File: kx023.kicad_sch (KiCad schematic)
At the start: 5 parts, among them U2001 KX023-1025-FR

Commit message: Schematic Changes
Added Manufacturer/MPN/Description Fields to parts
Added libraries to project
Modified FMC schematic to use new symbol
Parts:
- R2001, R2002: Manufacturer (none) -> YAGEO; Manufacturer Part Number (none) -> RC0603FR-074K75L
- U2001: Manufacturer (none) -> Kionix; Manufacturer Part Number (none) -> KX023-1025-FR
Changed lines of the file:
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@@
 			)
 		)
-		(property "Description" "Resistor"
+		(property "Description" "RES 4.75K OHM 1% 1/10W 0603"
 			(at 124.46 73.66 0)
 			(effects
@@
 		(property "Vendor" "digikey:311-4.75KHRCT-ND"
 			(at 248.92 0 0)
+			(effects
+				(font
+					(size 1.27 1.27)
+				)
+				(hide yes)
+			)
+		)
+		(property "Manufacturer" "YAGEO "
+			(at 124.46 73.66 0)
+			(effects
+				(font
+					(size 1.27 1.27)
+				)
+				(hide yes)
+			)
+		)
+		(property "Manufacturer Part Number" "RC0603FR-074K75L "
+			(at 124.46 73.66 0)
 			(effects
 				(font
@@
 			)
 		)
-		(property "Description" "Resistor"
+		(property "Description" "RES 4.75K OHM 1% 1/10W 0603"
 			(at 119.38 73.66 0)
 			(effects
@@
 		(property "Vendor" "digikey:311-4.75KHRCT-ND"
 			(at 238.76 0 0)
+			(effects
+				(font
+					(size 1.27 1.27)
+				)
+				(hide yes)
+			)
+		)
+		(property "Manufacturer" "YAGEO "
+			(at 119.38 73.66 0)
+			(effects
+				(font
+					(size 1.27 1.27)
+				)
+				(hide yes)
+			)
+		)
+		(property "Manufacturer Part Number" "RC0603FR-074K75L "
+			(at 119.38 73.66 0)
 			(effects
 				(font
@@
 			)
 		)
-		(property "Description" ""
+		(property "Description" "ACCELEROMETER 2-8G I2C/SPI 16LGA"
 			(at 139.7 82.55 0)
 			(effects
@@
 		(property "Vendor" "digikey:1191-1039-1-ND"
 			(at 0 165.1 0)
+			(effects
+				(font
+					(size 1.27 1.27)
+				)
+				(hide yes)
+			)
+		)
+		(property "Manufacturer" "Kionix"
+			(at 139.7 82.55 0)
+			(effects
+				(font
+					(size 1.27 1.27)
+				)
+				(hide yes)
+			)
+		)
+		(property "Manufacturer Part Number" "KX023-1025-FR "
+			(at 139.7 82.55 0)
 			(effects
 				(font
@@
 			)
 		)
+		(property "Manufacturer" ""
+			(at 109.22 83.82 0)
+			(effects
+				(font
+					(size 1.27 1.27)
+				)
+				(hide yes)
+			)
+		)
+		(property "Manufacturer Part Number" ""
+			(at 109.22 83.82 0)
+			(effects
+				(font
+					(size 1.27 1.27)
+				)
+				(hide yes)
+			)
+		)
 		(pin "1"
 		)
@@
 			(at 109.22 81.28 0)
 			(effects
+				(font
+					(size 1.27 1.27)
+				)
+				(hide yes)
+			)
+		)
+		(property "Manufacturer" ""
+			(at 109.22 81.28 0)
+			(effects
+				(font
+					(size 1.27 1.27)
+				)
+				(hide yes)
+			)
+		)
+		(property "Manufacturer Part Number" ""
+			(at 109.22 81.28 0)
+			(effects

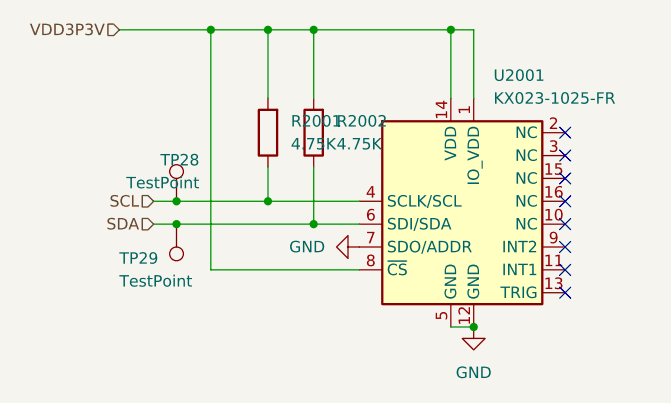
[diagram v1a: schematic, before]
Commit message: Properly attributed DNP parts; Added Fabrication Notes
-Properly attributed various DNP in the project;
This includes: C210.C710,C1601,C2502,C2602,L2501,R1507,L2601,R1601,R805
- I changed the accelerometer and microphone (+it's filter)to DNP parts
  Note: both of these are obsolete parts. As part of this change I Changed R1602 (part of mic buffer) from 220k to 0R. The removal of these parts should in no way negatively effect the rest of the circuit.
-I fixed the 'value' attribute of XMER2501&XMER2601 from 'TC4-6+' -> 'TC4-6T+'
- I added some fabrication notes to the F.Fab Layer
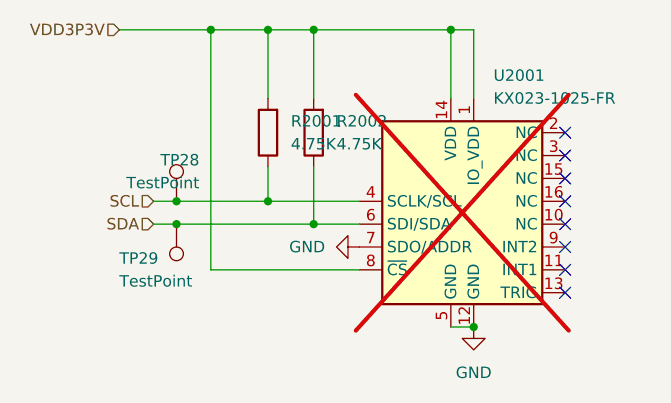
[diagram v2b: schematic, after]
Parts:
- U2001: now not fitted
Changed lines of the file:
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@@
 		(in_bom yes)
 		(on_board yes)
-		(dnp no)
+		(dnp yes)
 		(fields_autoplaced yes)
 		(property "Reference" "U2001"

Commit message: Changes to project for Final Review
- Changed R2001 & R2002 to DNP (these are accel. I2C pull ups)
- Added additional 100nF bypass caps to RF DAC on 1.8V and 3.3V rails [C1213,C1214]
- Added ORNL and Osprey Logo to Board
-Added Fab notes to F.Fab layer from the original PADS project
-- Adjusted Board stackup details to match these new notes

-Layout Tweaks/fixes:
- Deleted stray GND via under U1002 that is cutting up LMK2468_plane on In6.Cu
- Enlarged to 20mil LMK57_plane trace on In2.Cu (near U1002) (was12mil)
- Added second via to pin 6 of U1002 to LMK13_plane like others
- Added vias to VSS3P3V trace to connect to planes (starts near U3101)
- Added 4 GND vias under U2701 & U2901 (recommended layout has 6 ; had 1)
- Centered U701 pin 4 trace
- Make U701 traces to pins 45/46 smaller
- adjusted traces near 4 via clusters at U201 pins 45/46 and 3/4 to get rid of sharp corners
- centered U3201 pin 8/10/11 traces like U3101?
- U1201 pin 27, connected 2 VDD3P3V vias with trace on top layer
- U1201 pin 47, connected 3 VDD1P8V vias with trace on top layer
- Got rid of U1201 pin 56/57 via traces sharp corner, and added 2 additional vias like pins 71/72
- U1201: C1211 is 10uF for pins 56/57 and C1210 is 0.1uF for pins 71/72. Changed both to 0.1uF [adding C1213 mentioned eariler] and moved 10uF between the 2 0.1uF caps
- C1704 shown to U1701 pins 23/24 in sch but connected to U1201 pin 8 on PCB, and C201 close to U1701 pins 23/24 on PCB but connected to U201 pins 8/29 in sch (U701 has cap near pin 29 but U201 does not) - moveed caps to match sch and add bypass cap to U1201 DAC chip [C1214 mentioned earlier]

- It might be good to beef up the traces and number of vias to/from R901 and the In6.Cu plane for the VDD3P3V

-Regenerated all fabrication and documentation prints
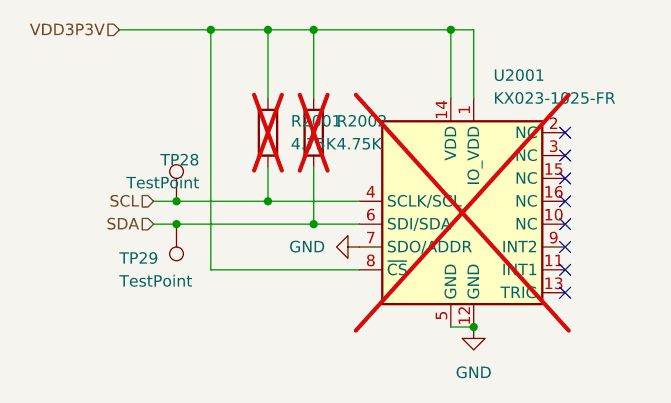
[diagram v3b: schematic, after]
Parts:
- R2001, R2002: now not fitted
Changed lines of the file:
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@@
 		(in_bom yes)
 		(on_board yes)
-		(dnp no)
+		(dnp yes)
 		(fields_autoplaced yes)
 		(property "Reference" "R2002"
@@
 		(in_bom yes)
 		(on_board yes)
-		(dnp no)
+		(dnp yes)
 		(fields_autoplaced yes)
 		(property "Reference" "R2001"
